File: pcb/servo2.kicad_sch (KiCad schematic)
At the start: 35 parts, among them J19 Feeder 17, J20 Feeder 18, J21 Feeder 19, J22 Feeder 20, J23 Feeder 21, J24 Feeder 22, J25 Feeder 23, J26 Feeder 24, J27 Feeder 25, J28 Feeder 26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

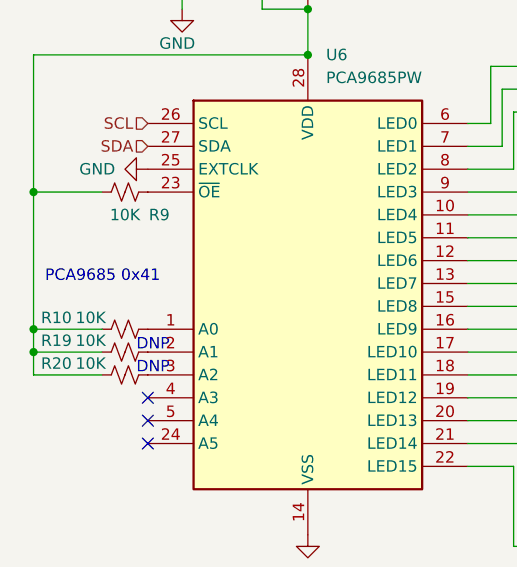
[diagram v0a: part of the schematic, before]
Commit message: Exclude R3 and R9 from population.
Upgrades files to KiCad 7.x.

Fixes: https://github.com/atanisoft/Esp32FeederController/issues/10
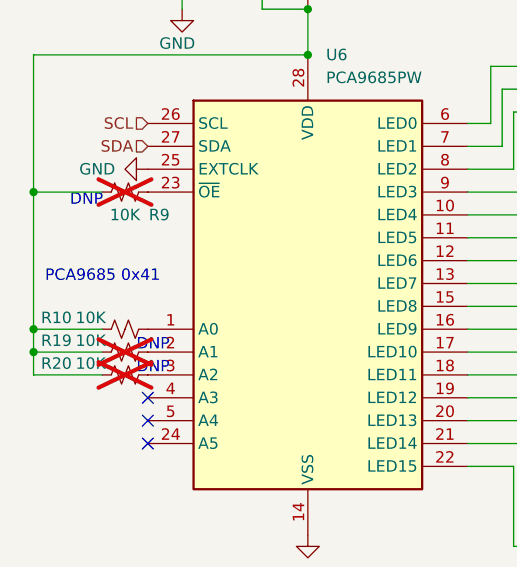
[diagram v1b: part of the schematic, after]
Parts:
- R19, R20, R9: now not fitted; now left out of the parts list
